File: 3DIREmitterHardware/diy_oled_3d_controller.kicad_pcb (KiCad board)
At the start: 2 copper layers, 37.5 x 59.1 mm, 20 parts, among them Q1 AO3400A, U1 OPT101P, U2 OPT101P

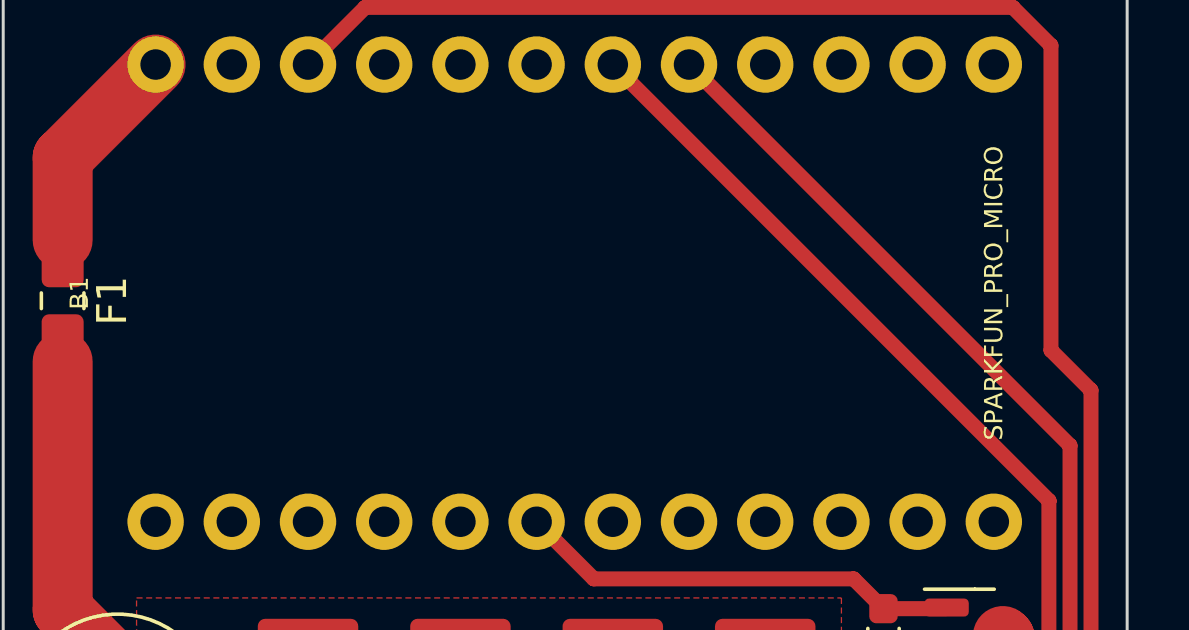
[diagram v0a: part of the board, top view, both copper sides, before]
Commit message: added license text to PCB model
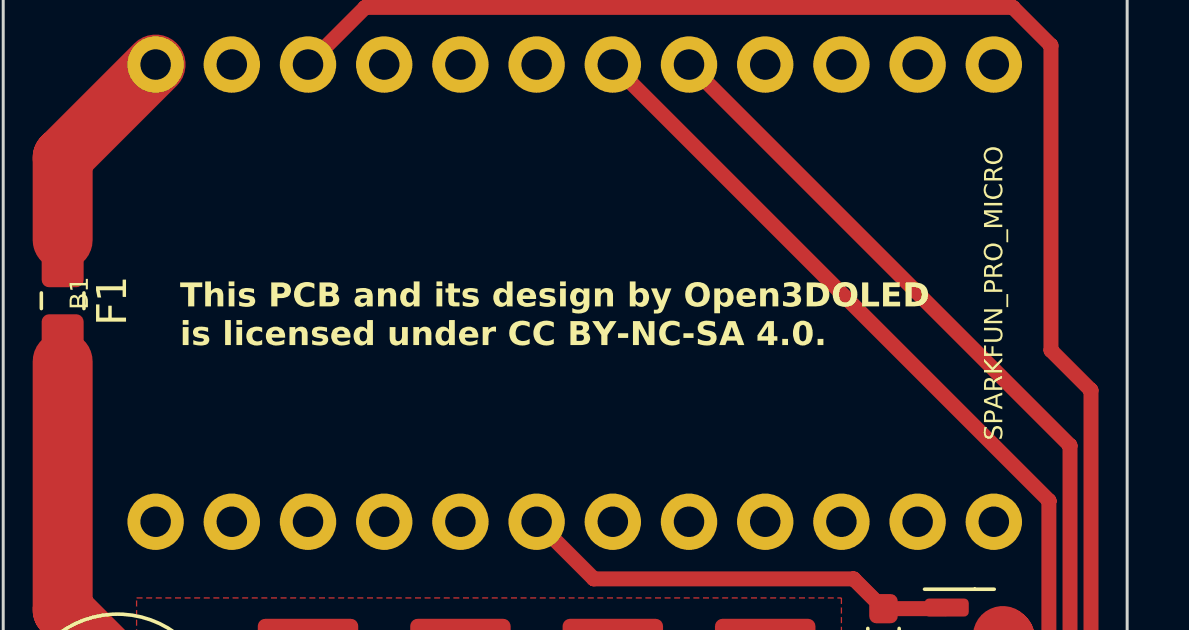
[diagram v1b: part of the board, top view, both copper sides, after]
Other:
- board text added: "This PCB and its design by Open3DOLED is licensed under CC BY-NC-SA 4.0."
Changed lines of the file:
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@@
   (gr_line (start 91.44 48.895) (end 128.905 48.895)
     (stroke (width 0.1) (type solid)) (layer "Edge.Cuts"))
+  (gr_text "This PCB and its design by Open3DOLED \nis licensed under CC BY-NC-SA 4.0." (at 122.428 61.468) (layer "B.SilkS")
+    (effects (font (size 0.8 0.8) (thickness 0.2) bold) (justify left bottom mirror))
+  )
+  (gr_text "This PCB and its design by Open3DOLED \nis licensed under CC BY-NC-SA 4.0." (at 97.3328 61.5188) (layer "F.SilkS")
+    (effects (font (size 0.8 0.8) (thickness 0.2) bold) (justify left bottom))
+  )
   (segment (start 122.85 70.2075) (end 122.8875 70.17) (width 0.5) (layer "F.Cu") (net 6))
   (segment (start 109.22 67.31) (end 111.125 69.215) (width 0.5) (layer "F.Cu") (net 6))

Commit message: fixed fillzone in hardware pcb design wasn't connected to 5V_AFTER_FUSE
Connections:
- B1 pad 24: Net-(C1-Pad1) -> +5V
- C1 pad 1: Net-(C1-Pad1) -> /5V_AFTER_FUSE
- F1 pad 1: Net-(C1-Pad1) -> +5V
- F1 pad 2: Net-(C1-Pad1) -> /5V_AFTER_FUSE
- R10 pad 1: Net-(C1-Pad1) -> /5V_AFTER_FUSE
- R11 pad 1: Net-(C1-Pad1) -> /5V_AFTER_FUSE
- R12 pad 1: Net-(C1-Pad1) -> /5V_AFTER_FUSE
- R13 pad 1: Net-(C1-Pad1) -> /5V_AFTER_FUSE
- U1 pad 1: Net-(C1-Pad1) -> /5V_AFTER_FUSE
- U2 pad 1: Net-(C1-Pad1) -> /5V_AFTER_FUSE
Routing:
- net Net-(C1-Pad1): track 76.8 -> 0.00 mm
- net /5V_AFTER_FUSE: track 0.00 -> 69.7 mm
- net +5V: track 0.00 -> 7.13 mm
- added copper zone on F.Cu, net /5V_AFTER_FUSE
- removed copper zone on F.Cu, net +5V
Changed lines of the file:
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@@
   (net 23 "+5V")
   (net 24 "Net-(B1-RESET)")
-  (net 25 "Net-(C1-Pad1)")
+  (net 25 "/5V_AFTER_FUSE")
   (net 26 "unconnected-(U1--IN-Pad2)")
   (net 27 "/LED_MOSFET")
@@
       (stroke (width 0.1) (type solid)) (layer "F.Fab"))
     (pad "1" smd roundrect (at -1.025 0 270) (size 1.15 1.4) (layers "F.Cu" "F.Paste" "F.Mask") (roundrect_rratio 0.2173913043)
-      (net 25 "Net-(C1-Pad1)") (pintype "passive"))
+      (net 23 "+5V") (pintype "passive"))
     (pad "2" smd roundrect (at 1.025 0 270) (size 1.15 1.4) (layers "F.Cu" "F.Paste" "F.Mask") (roundrect_rratio 0.2173913043)
-      (net 25 "Net-(C1-Pad1)") (pintype "passive"))
+      (net 25 "/5V_AFTER_FUSE") (pintype "passive"))
     (model "${KICAD6_3DMODEL_DIR}/Fuse.3dshapes/Fuse_0805_2012Metric.wrl"
       (offset (xyz 0 0 0))
@@
       (stroke (width 0.1) (type solid)) (layer "F.Fab"))
     (pad "1" smd roundrect (at -3.05 0 270) (size 1.4 3.35) (layers "F.Cu" "F.Paste" "F.Mask") (roundrect_rratio 0.1785707143)
-      (net 25 "Net-(C1-Pad1)") (pintype "passive"))
+      (net 25 "/5V_AFTER_FUSE") (pintype "passive"))
     (pad "2" smd roundrect (at 3.05 0 270) (size 1.4 3.35) (layers "F.Cu" "F.Paste" "F.Mask") (roundrect_rratio 0.1785707143)
       (net 28 "/RESISTOR_LED") (pintype "passive"))
@@
       (stroke (width 0.1) (type solid)) (fill none) (layer "F.Fab"))
     (pad "1" thru_hole circle (at 0 0 180) (size 1.6 1.6) (drill 0.8) (layers "*.Cu" "*.Mask")
-      (net 25 "Net-(C1-Pad1)") (pintype "passive"))
+      (net 25 "/5V_AFTER_FUSE") (pintype "passive"))
     (pad "2" thru_hole circle (at 2.5 0 180) (size 1.6 1.6) (drill 0.8) (layers "*.Cu" "*.Mask")
       (net 22 "GND") (pintype "passive"))
@@
       (net 22 "GND") (pinfunction "GND") (pintype "power_in") (solder_mask_margin 0.1016))
     (pad "24" thru_hole circle (at 7.62 -12.7 90) (size 1.8796 1.8796) (drill 1.016) (layers "*.Cu" "*.Mask")
-      (net 25 "Net-(C1-Pad1)") (pinfunction "RAW") (pintype "power_in") (solder_mask_margin 0.1016))
+      (net 23 "+5V") (pinfunction "RAW") (pintype "power_in") (solder_mask_margin 0.1016))
   )
   (footprint "LED_THT:LED_D5.0mm" (layer "F.Cu")
@@
       (stroke (width 0.1) (type solid)) (layer "F.Fab"))
     (pad "1" smd roundrect (at -3.05 0 270) (size 1.4 3.35) (layers "F.Cu" "F.Paste" "F.Mask") (roundrect_rratio 0.1785707143)
-      (net 25 "Net-(C1-Pad1)") (pintype "passive"))
+      (net 25 "/5V_AFTER_FUSE") (pintype "passive"))
     (pad "2" smd roundrect (at 3.05 0 270) (size 1.4 3.35) (layers "F.Cu" "F.Paste" "F.Mask") (roundrect_rratio 0.1785707143)
       (net 28 "/RESISTOR_LED") (pintype "passive"))
@@
       (stroke (width 0.1) (type solid)) (layer "F.Fab"))
     (pad "1" smd roundrect (at -3.05 0 270) (size 1.4 3.35) (layers "F.Cu" "F.Paste" "F.Mask") (roundrect_rratio 0.1785707143)
-      (net 25 "Net-(C1-Pad1)") (pintype "passive"))
+      (net 25 "/5V_AFTER_FUSE") (pintype "passive"))
     (pad "2" smd roundrect (at 3.05 0 270) (size 1.4 3.35) (layers "F.Cu" "F.Paste" "F.Mask") (roundrect_rratio 0.1785707143)
       (net 28 "/RESISTOR_LED") (pintype "passive"))
@@
       (stroke (width 0.1) (type solid)) (layer "F.Fab"))
     (pad "1" smd roundrect (at -3.05 0 270) (size 1.4 3.35) (layers "F.Cu" "F.Paste" "F.Mask") (roundrect_rratio 0.1785707143)
-      (net 25 "Net-(C1-Pad1)") (pintype "passive"))
+      (net 25 "/5V_AFTER_FUSE") (pintype "passive"))
     (pad "2" smd roundrect (at 3.05 0 270) (size 1.4 3.35) (layers "F.Cu" "F.Paste" "F.Mask") (roundrect_rratio 0.1785707143)
       (net 28 "/RESISTOR_LED") (pintype "passive"))
@@
       (stroke (width 0.2) (type solid)) (fill none) (layer "B.Fab"))
     (pad "1" thru_hole rect (at -3.815 3.81 180) (size 1.22 1.22) (drill 0.87) (layers "*.Cu" "*.Mask")
-      (net 25 "Net-(C1-Pad1)") (pinfunction "VS") (pintype "power_in"))
+      (net 25 "/5V_AFTER_FUSE") (pinfunction "VS") (pintype "power_in"))
     (pad "2" thru_hole circle (at -3.815 1.27 180) (size 1.22 1.22) (drill 0.87) (layers "*.Cu" "*.Mask")
       (net 29 "unconnected-(U2--IN-Pad2)") (pinfunction "-IN") (pintype "input"))
@@
       (stroke (width 0.2) (type solid)) (fill none) (layer "B.Fab"))
     (pad "1" thru_hole rect (at -3.815 3.81 180) (size 1.22 1.22) (drill 0.87) (layers "*.Cu" "*.Mask")
-      (net 25 "Net-(C1-Pad1)") (pinfunction "VS") (pintype "power_in"))
+      (net 25 "/5V_AFTER_FUSE") (pinfunction "VS") (pintype "power_in"))
     (pad "2" thru_hole circle (at -3.815 1.27 180) (size 1.22 1.22) (drill 0.87) (layers "*.Cu" "*.Mask")
       (net 26 "unconnected-(U1--IN-Pad2)") (pinfunction "-IN") (pintype "input"))
@@
   (via (at 120.65 76.2) (size 0.8) (drill 0.4) (layers "F.Cu" "B.Cu") (free) (net 22))
   (via (at 120.65 74.295) (size 0.8) (drill 0.4) (layers "F.Cu" "B.Cu") (net 22))
+  (segment (start 93.4212 55.1688) (end 96.52 52.07) (width 2) (layer "F.Cu") (net 23))
+  (segment (start 93.4212 57.919) (end 93.4212 55.1688) (width 2) (layer "F.Cu") (net 23))
   (segment (start 127.69952 62.92952) (end 127.69952 104.71048) (width 0.5) (layer "F.Cu") (net 24))
   (segment (start 103.505 50.165) (end 125.095 50.165) (width 0.5) (layer "F.Cu") (net 24))
@@
   (segment (start 115.55 106.68) (end 113.005 104.135) (width 0.5) (layer "F.Cu") (net 24))
   (segment (start 125.73 106.68) (end 115.55 106.68) (width 0.5) (layer "F.Cu") (net 24))
-  (segment (start 93.4212 55.1688) (end 96.52 52.07) (width 2) (layer "F.Cu") (net 25))
   (segment (start 94.551929 96.52) (end 100.33 96.52) (width 1) (layer "F.Cu") (net 25))
   (segment (start 92.705 94.673071) (end 94.551929 96.52) (width 1) (layer "F.Cu") (net 25))
@@
   (segment (start 92.71 94.668071) (end 92.705 94.673071) (width 1) (layer "F.Cu") (net 25))
   (segment (start 100.33 96.52) (end 101.6 97.79) (width 1) (layer "F.Cu") (net 25))
-  (segment (start 93.4212 57.919) (end 93.4212 55.1688) (width 2) (layer "F.Cu") (net 25))
   (segment (start 96.5 73.331572) (end 96.5 73.66) (width 2) (layer "F.Cu") (net 25))
   (segment (start 101.6 97.79) (end 102.909511 96.480489) (width 1) (layer "B.Cu") (net 25))
@@
   (via (at 123.825 76.2) (size 0.8) (drill 0.4) (layers "F.Cu" "B.Cu") (net 27))
   (via (at 123.825 77.47) (size 0.8) (drill 0.4) (layers "F.Cu" "B.Cu") (net 27))
-  (zone (net 23) (net_name "+5V") (layer "F.Cu") (hatch edge 0.508)
+  (zone (net 25) (net_name "/5V_AFTER_FUSE") (layer "F.Cu") (hatch edge 0.508)
     (priority 1)
     (connect_pads yes (clearance 0.508))

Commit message: initial v2 pcb hardware design
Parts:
- removed D5, D6, D7, D8: LED, LED_THT:LED_D5.0mm
- added C2: C_Polarized, Capacitor_THT:C_Radial_D6.3mm_H11.0mm_P2.50mm, F.Cu at (123.5, 78.5)
- added C3: 100nF, Capacitor_SMD:C_0603_1608Metric_Pad1.08x0.95mm_HandSolder, F.Cu at (109.5, 102.4)
- added C4: 100nF, Capacitor_SMD:C_0603_1608Metric_Pad1.08x0.95mm_HandSolder, F.Cu at (99.5, 100.9)
- added D10: VBPW34S, VBPW34S:XDCR_VBPW34S, B.Cu at (97.0, 106.0)
- added D11: LED, LED_SMD:LED_1210_3225Metric_Pad1.42x2.65mm_HandSolder, F.Cu at (94.1, 119.5)
- added D12: LED, LED_SMD:LED_1210_3225Metric_Pad1.42x2.65mm_HandSolder, F.Cu at (99.0, 119.5)
- added D13: LED, LED_SMD:LED_1210_3225Metric_Pad1.42x2.65mm_HandSolder, F.Cu at (104.0, 119.5)
- added D14: LED, LED_SMD:LED_1210_3225Metric_Pad1.42x2.65mm_HandSolder, F.Cu at (109.0, 119.5)
- added D9: VBPW34S, VBPW34S:XDCR_VBPW34S, B.Cu at (112.1, 106.0)
- added H1: MountingHole, Library:MountingHole_1.6mm_M1.4_ISO7380, F.Cu at (95.0, 37.5)
- added H2: MountingHole, Library:MountingHole_1.6mm_M1.4_ISO7380, F.Cu at (122.5, 71.5)
- added H3: MountingHole, Library:MountingHole_1.6mm_M1.4_ISO7380, F.Cu at (95.0, 88.5)
- added H4: MountingHole, Library:MountingHole_1.6mm_M1.4_ISO7380, F.Cu at (104.5, 106.5)
- added H5: MountingHole, Library:MountingHole_1.6mm_M1.4_ISO7380, F.Cu at (95.0, 113.0)
- added H6: MountingHole, Library:MountingHole_1.6mm_M1.4_ISO7380, F.Cu at (104.5, 131.0)
- added J1: Conn_01x06_Pin, Connector_PinHeader_2.54mm:PinHeader_1x06_P2.54mm_Vertical, F.Cu at (101.0, 81.5)
- added J2: Conn_01x06_Pin, Connector_PinHeader_2.54mm:PinHeader_1x06_P2.54mm_Vertical, F.Cu at (101.0, 88.0)
- added J3: Conn_01x06_Pin, Connector_PinHeader_2.54mm:PinHeader_1x06_P2.54mm_Vertical, F.Cu at (101.0, 112.5)
- added Q2: AO3400A, Package_TO_SOT_SMD:SOT-23, F.Cu at (114.0, 120.4)
- added R2: 10k, Resistor_SMD:R_0603_1608Metric_Pad0.98x0.95mm_HandSolder, F.Cu at (111.5, 102.4)
- added R3: 10k, Resistor_SMD:R_0603_1608Metric_Pad0.98x0.95mm_HandSolder, F.Cu at (97.5, 100.9)
- added R4: 1000, Resistor_SMD:R_0603_1608Metric_Pad0.98x0.95mm_HandSolder, F.Cu at (114.1, 117.5)
- added S2: TL3342F160QG, Tactile.Switch:SW_TL3342F160QG, F.Cu at (99.3, 50.2)
- added S3: TL3342F160QG, Tactile.Switch:SW_TL3342F160QG, F.Cu at (99.3, 57.3)
- added S4: TL3342F160QG, Tactile.Switch:SW_TL3342F160QG, F.Cu at (99.3, 64.3)
- added U4: MCP6022-I_SN, MCP6022-I_SN:SOIC127P599X175-8N, F.Cu at (104.5, 102.0)
- D1, D2, D3, D4: footprint LED_THT:LED_D5.0mm -> LED_SMD:LED_1210_3225Metric_Pad1.42x2.65mm_HandSolder
- moved S1 60.1 mm to (99.3, 43.1)
- moved U2 27.3 mm to (112.0, 127.5)
- moved Q1 27.1 mm to (111.9, 95.4), turned to -90 degrees
- moved U1 25.9 mm to (97.0, 127.5)
- moved R1 23.1 mm to (111.9, 92.5), turned to 180 degrees
- moved D4 18.2 mm to (107.5, 95.5)
- moved D3 15.4 mm to (103.0, 95.5)
- moved D2 13.0 mm to (98.5, 95.5)
- moved D1 11.5 mm to (94.0, 95.5)
- moved B1 10.7 mm to (115.6, 51.1), turned to 0 degrees
- moved F1 10.7 mm to (97.0, 70.0), turned to 0 degrees
- moved C1 4.84 mm to (96.5, 78.5)
- moved R10 1.50 mm to (116.7, 72.8)
- moved R11 1.50 mm to (111.7, 72.8)
- moved R12 1.50 mm to (106.6, 72.8)
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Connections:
- net +5V renamed +5V_1
- net /LED_MOSFET renamed /LED_MOSFET_2
- B1 pad 17: /RIGHT_OPT101_OUTPUT -> /RIGHT_SIGNAL_1
- B1 pad 18: /LEFT_OPT101_OUTPUT -> /LEFT_SIGNAL_1
- B1 pad 21: unconnected-(B1-VCC-Pad21) -> /VCC_1
- B1 pad 23: GND -> GND1
- B1 pad 5: unconnected-(B1-2-Pad5) -> Net-(B1-2)
- B1 pad 6: /LED_CONTROL -> /LED_CONTROL_1
- B1 pad 7: unconnected-(B1-4-Pad7) -> Net-(B1-4)
- B1 pad 8: unconnected-(B1-*5-Pad8) -> Net-(B1-*5)
- C1 pad 2: GND -> GND1
- D1 pad 2: /RESISTOR_LED -> /LED_POWER_2
- D2 pad 2: /RESISTOR_LED -> /LED_POWER_2
- D3 pad 2: /RESISTOR_LED -> /LED_POWER_2
- D4 pad 2: /RESISTOR_LED -> /LED_POWER_2
- Q1 pad 1: /LED_CONTROL -> /LED_CONTROL_2
- Q1 pad 2: GND -> GND2
- R1 pad 1: /LED_CONTROL -> /LED_CONTROL_2
- R1 pad 2: GND -> GND2
- R10 pad 2: /RESISTOR_LED -> /LED_POWER_1
- R11 pad 2: /RESISTOR_LED -> /LED_POWER_1
- R12 pad 2: /RESISTOR_LED -> /LED_POWER_1
- R13 pad 2: /RESISTOR_LED -> /LED_POWER_1
- S1 pad 3: GND -> GND1
- S1 pad 4: GND -> GND1
- U1 pad 1: /5V_AFTER_FUSE -> /VCC_3
- U1 pad 3: GND -> GND3
- U1 pad 4: /LEFT_OPT101_OUTPUT -> /LEFT_SIGNAL_3
- U1 pad 5: /LEFT_OPT101_OUTPUT -> /LEFT_SIGNAL_3
- U1 pad 8: GND -> GND3
- U2 pad 1: /5V_AFTER_FUSE -> /VCC_3
- U2 pad 3: GND -> GND3
- U2 pad 4: /RIGHT_OPT101_OUTPUT -> /RIGHT_SIGNAL_3
- U2 pad 5: /RIGHT_OPT101_OUTPUT -> /RIGHT_SIGNAL_3
- U2 pad 8: GND -> GND3
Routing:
- net /LEFT_OPT101_OUTPUT: track 90.2 -> 0.00 mm
- net /RIGHT_OPT101_OUTPUT: track 67.3 -> 0.00 mm
- net Net-(B1-RESET): track 102.8 -> 37.0 mm
- net /VCC_1: track 0.00 -> 54.9 mm
- net +5V_1: track 7.13 -> 59.6 mm, vias 0 -> 1
- net /5V_AFTER_FUSE: track 69.7 -> 29.5 mm
- net /LEFT_SIGNAL_3: track 0.00 -> 37.3 mm
- net /LED_CONTROL_1: track 0.00 -> 34.7 mm
- net /LEFT_SIGNAL_1: track 0.00 -> 32.8 mm
- net /RIGHT_SIGNAL_1: track 0.00 -> 29.3 mm
- net /RIGHT_SIGNAL_3: track 0.00 -> 27.3 mm
- net /VCC_3: track 0.00 -> 26.6 mm, vias 0 -> 2
- net /LEFT_SIGNAL_2: track 0.00 -> 24.7 mm, vias 0 -> 1
- net /RIGHT_SIGNAL_2: track 0.00 -> 22.5 mm, vias 0 -> 1
- net /LED_POWER_3: track 0.00 -> 21.2 mm
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- added copper zone on B.Cu, net GND1
- added copper zone on F.Cu, net GND1
- added copper zone on B.Cu, net GND2
- added copper zone on F.Cu, net GND2
- added copper zone on B.Cu, net GND3
- added copper zone on F.Cu, net GND3
- removed copper zone on F.Cu, net /5V_AFTER_FUSE
- removed copper zone on B.Cu, net /LED_MOSFET_2
- removed copper zone on F.Cu, net /RESISTOR_LED
- removed copper zone on B.Cu, net GND
- removed copper zone on F.Cu, net GND
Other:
- board size 37.5 x 59.1 mm -> 37.5 x 99 mm

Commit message: some minor fixes to pcb schamtic values for opamp passives
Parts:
- C3, C4: value 100nF -> 47pF
- R2, R3: value 10k -> 510k
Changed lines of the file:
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@@
 			)
 		)
-		(property "Value" "100nF"
+		(property "Value" "47pF"
 			(at 0 1.43 90)
 			(layer "F.Fab")
@@
 			)
 		)
-		(property "Value" "100nF"
+		(property "Value" "47pF"
 			(at 0 1.43 -90)
 			(layer "F.Fab")
@@
 			)
 		)
-		(property "Value" "10k"
+		(property "Value" "510k"
 			(at 0 1.43 -90)
 			(layer "F.Fab")
@@
 			)
 		)
-		(property "Value" "10k"
+		(property "Value" "510k"
 			(at 0 1.43 90)
 			(layer "F.Fab")
